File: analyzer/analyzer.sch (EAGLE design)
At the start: 30 parts, among them IC1 FT230XS, J4 ICSP, Q1 16MHz, U1 ATA6631, U2 ATMEGA328P, U4 TLP291, X2 USB-SMD-NS

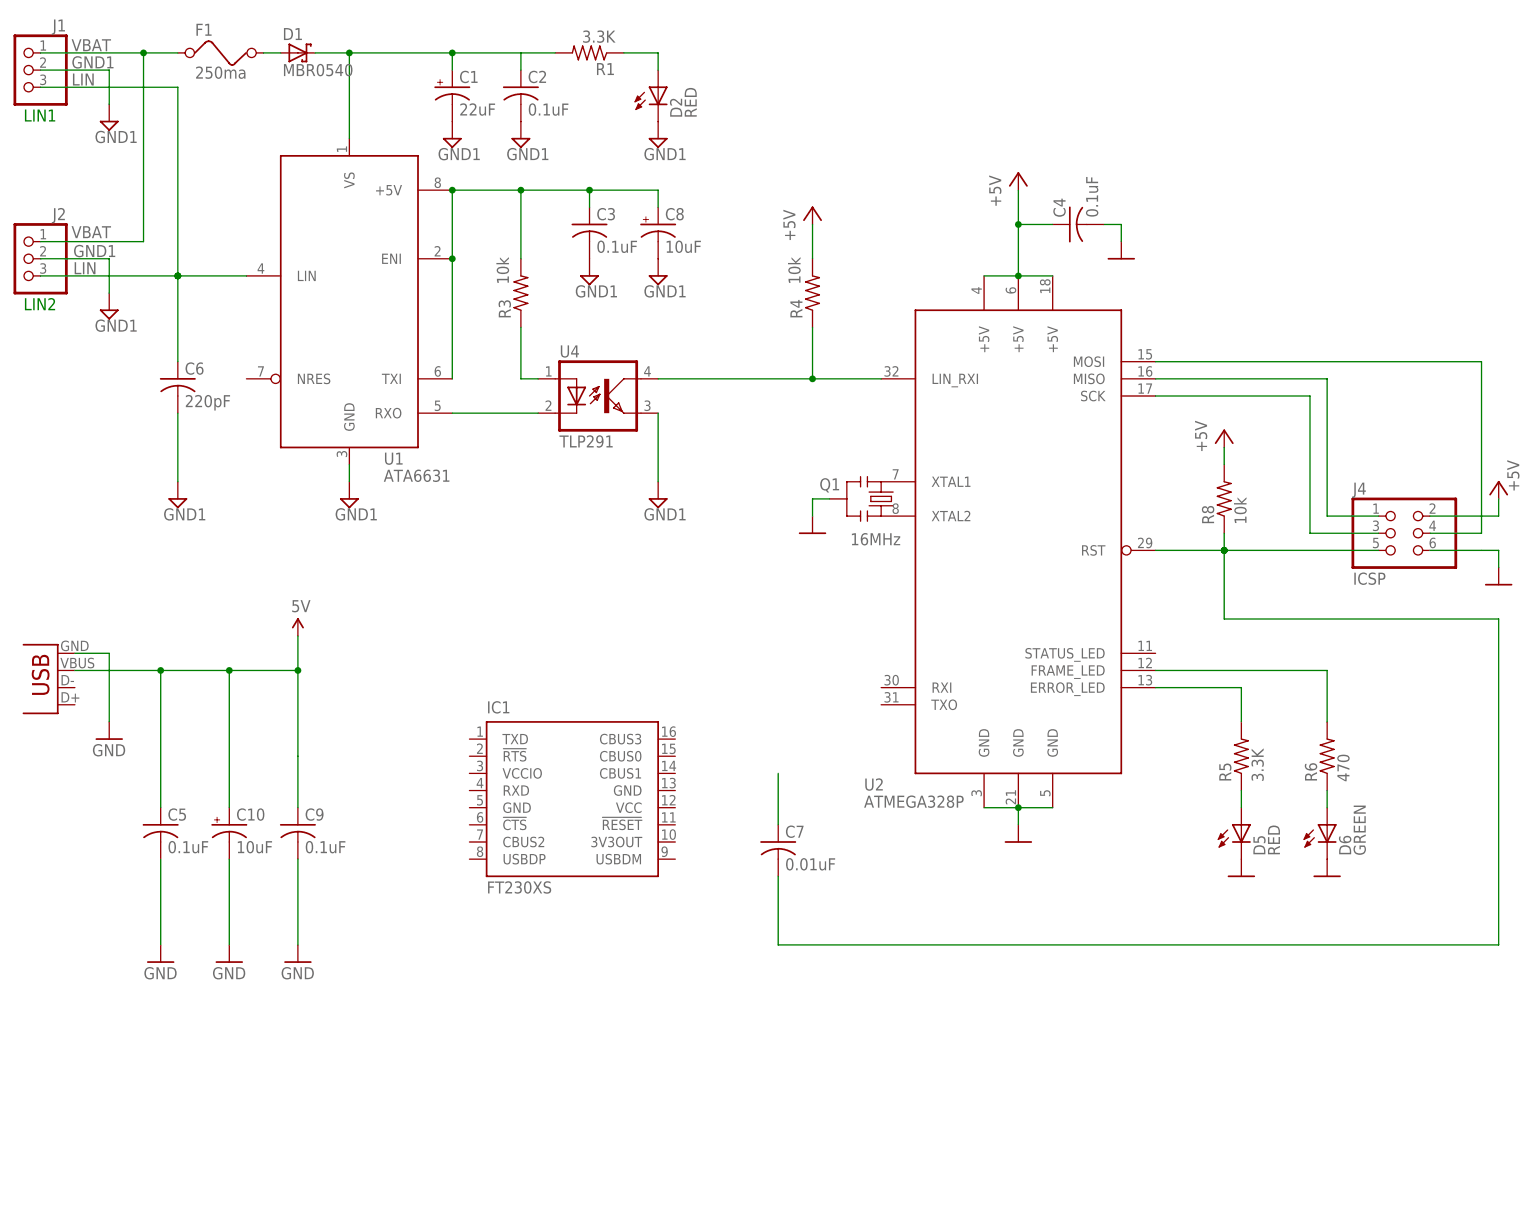
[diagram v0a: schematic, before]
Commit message: Analyzer now can transmit signals to the linbus. Not used yet by the software.
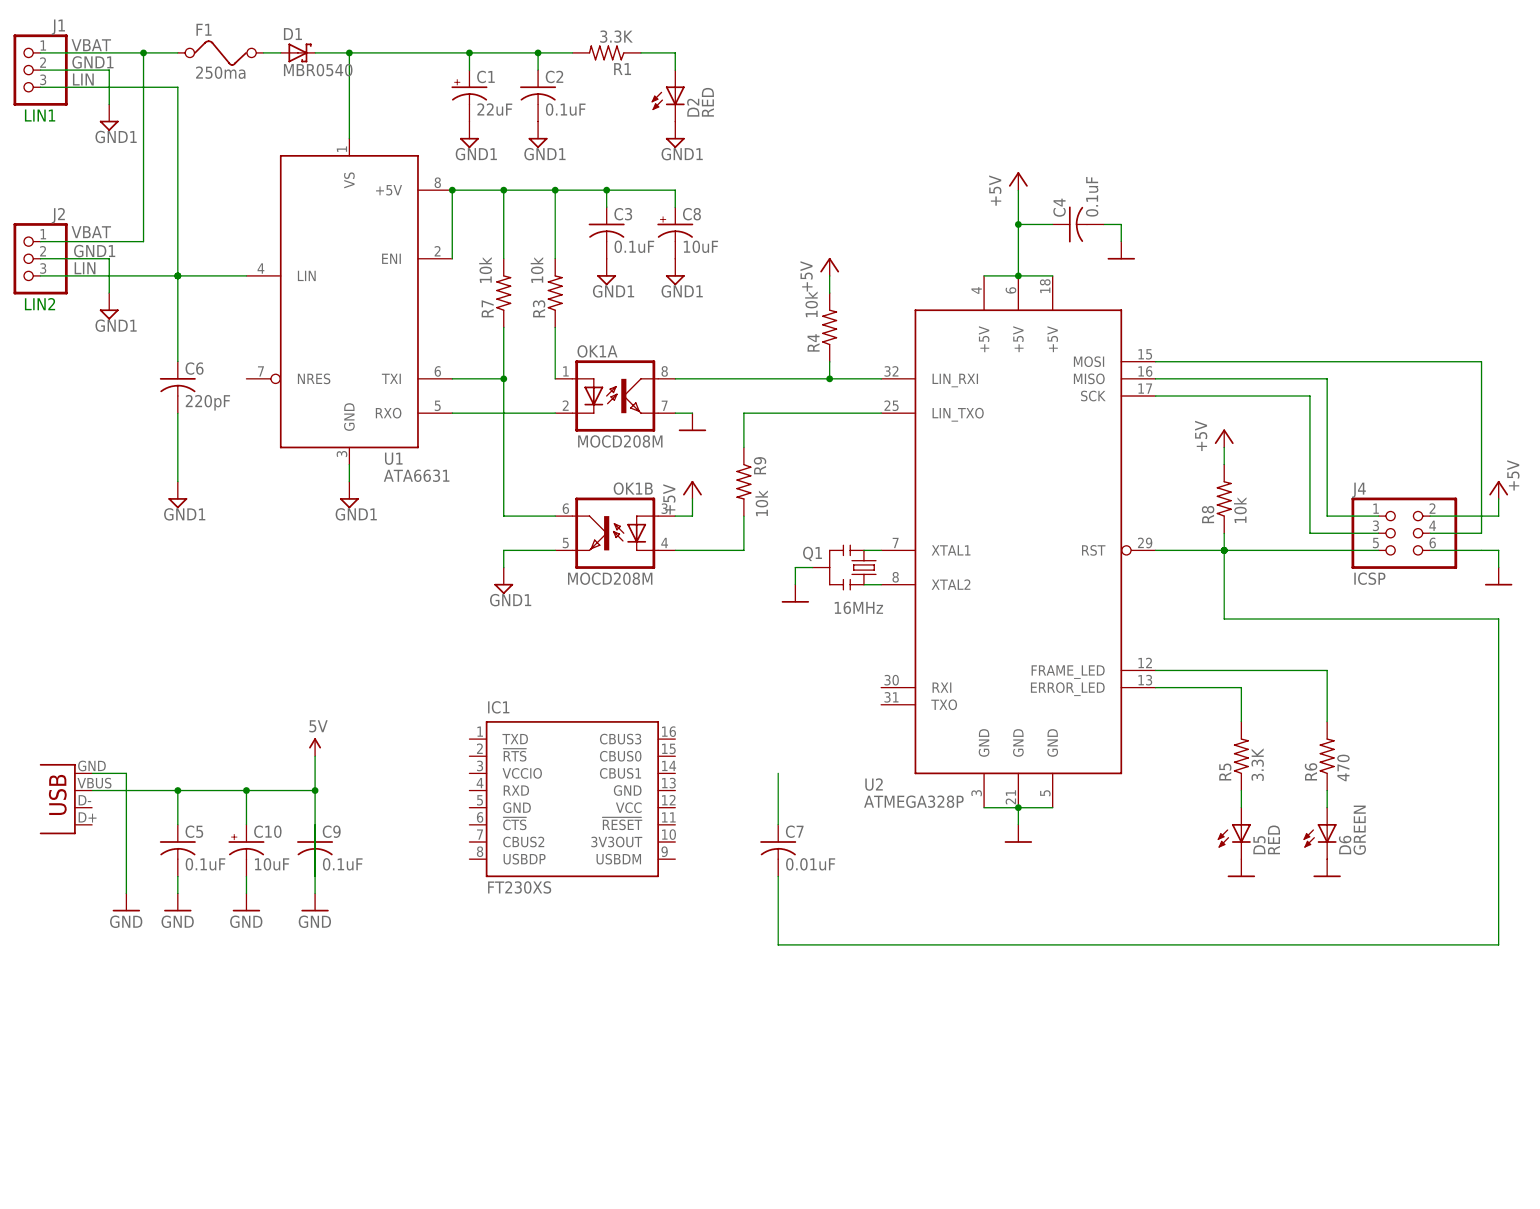
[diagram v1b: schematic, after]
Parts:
- removed U4: TLP291, optocoupler:TLP283
- added OK1: MOCD208M, optocoupler:MOCD208M
- added R7, R9: 10k, rcl:R-US_R0805
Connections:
- new net N$12: OK1B.C, R9.2
- new net N$2: R9.1
- new net N$9: OK1B.COL, R7.1, U1.TXI
- net +5V: now also OK1B.A, R7.2; no longer U1.TXI
- net GND: now also OK1A.EMIT
- net GND1: now also OK1B.EMIT; no longer U4.EMIT
- net N$1: now also OK1A.A; no longer U4.A
- net N$10: now also OK1A.COL; no longer U4.COL
- net N$5: now also OK1A.C; no longer U4.C
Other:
- moved on the sheet: C1, C10, C2, C3, C5, C8, C9, D2, Q1, R1, R3, R4

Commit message: Refactored the analyzer schema.
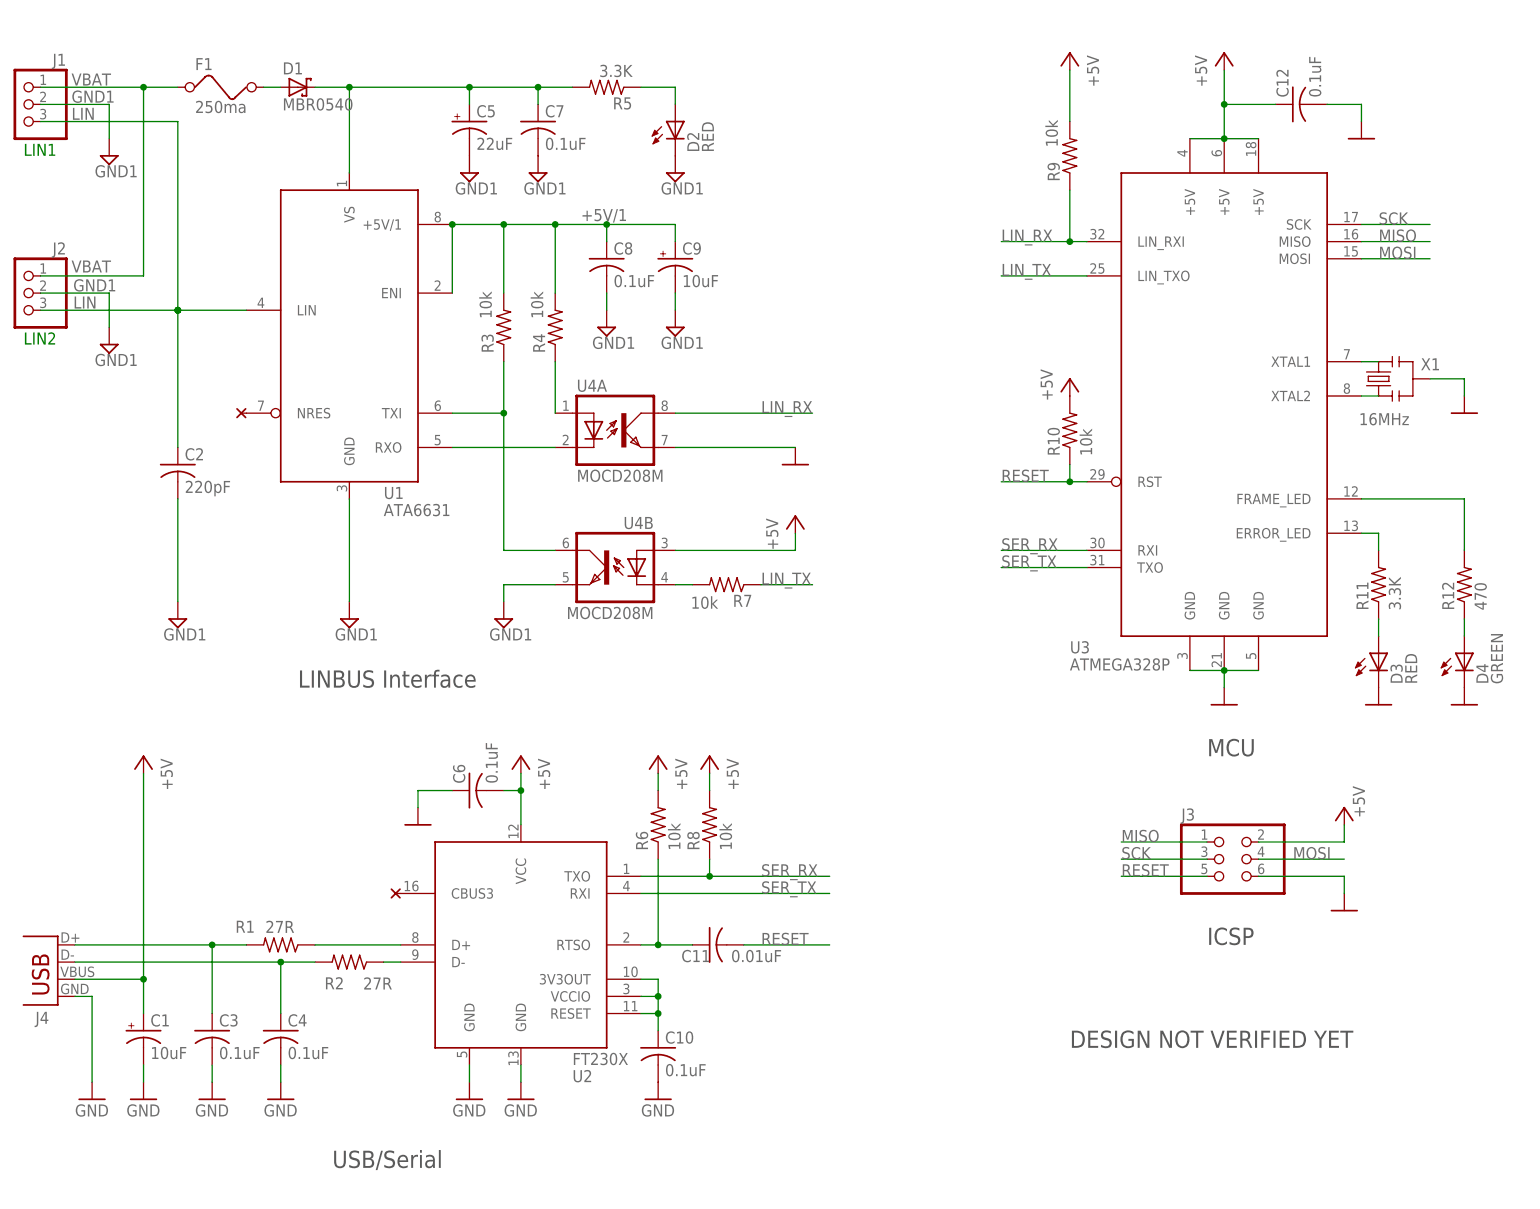
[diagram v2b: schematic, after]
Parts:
- removed D5: RED, led:LEDSMT1206
- removed D6: GREEN, led:LEDSMT1206
- removed IC1: FT230XS, ftdichip:FT230XS
- removed OK1: MOCD208M, optocoupler:MOCD208M
- removed Q1: 16MHz, analyzer:RESONATORSMD
- removed X2: USB-SMD-NS, SparkFun:USB-SMD-NS
- added C11: 0.01uF, rcl:C-USC0805
- added C12: 0.1uF, rcl:C-USC0805
- added D3: RED, led:LEDSMT1206
- added D4: GREEN, led:LEDSMT1206
- added J3: (no value), pinhead:PINHD-2X3
- added R10: 10k, rcl:R-US_R0805
- added R11: 3.3K, rcl:R-US_R0805
- added R12: 470, rcl:R-US_R0805
- added R2: 27R, rcl:R-US_R0805
- added U3: ATMEGA328P, analyzer:ATMEGA328P
- added U4: MOCD208M, optocoupler:MOCD208M
- added X1: 16MHz, analyzer:RESONATORSMD
- C1: value 22uF -> 10uF; device rcl:CPOL-USUD-6,3X5,8 -> rcl:CPOL-USA/3216-18R
- C10, C8: value 10uF -> 0.1uF; device rcl:CPOL-USA/3216-18R -> rcl:C-USC0805
- C2: value 0.1uF -> 220pF
- C5: value 0.1uF -> 22uF; device rcl:C-USC0805 -> rcl:CPOL-USUD-6,3X5,8
- C6: value 220pF -> 0.1uF
- C7: value 0.01uF -> 0.1uF
- C9: value 0.1uF -> 10uF; device rcl:C-USC0805 -> rcl:CPOL-USA/3216-18R
- J4: value ICSP -> USBSMD; device pinhead:PINHD-2X3 -> analyzer:USBSMD
- R1: value 3.3K -> 27R
- R6: value 470 -> 10k
- U2: value ATMEGA328P -> FT230X; device analyzer:ATMEGA328P -> analyzer:FT230X
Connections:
- removed net 3.3V: C9.1
- removed net N$2: R9.1
- removed net N$25: J4.1, U2.MISO
- removed net N$28: J4.3, U2.SCK
- removed net XTAL1: Q1.3, U2.XTAL1
- removed net XTAL2: Q1.1, U2.XTAL2
- new net +5V/1: C8.1, C9.+, R3.2, R4.2, U1.+5V/1, U1.ENI
- new net LIN_RX: R9.1, U3.LIN_RXI, U4A.COL
- new net LIN_TX: R7.1, U3.LIN_TXO
- new net MISO: J3.1, U3.MISO
- new net MOSI: J3.4, U3.MOSI
- new net N$13: U3.XTAL1, X1.3
- new net N$14: U3.XTAL2, X1.1
- new net N$15: C4.1, J4.D-, R2.2
- new net N$18: C10.1, U2.3V3OUT, U2.RESET, U2.VCCIO
- new net RESET: C11.2, J3.5, R10.1, U3.RST
- new net SCK: J3.3, U3.SCK
- new net SER_RX: R8.1, U2.TXO, U3.RXI
- new net SER_TX: U2.RXI, U3.TXO
- net +12V: now also C5.+, C7.1, R5.2; no longer C1.+, C2.1, R1.2
- net +5V: now also C1.+, C12.1, C6.2, J3.2, J4.VBUS, R10.2, R6.2, R9.2, U2.VCC, U3.+5V@1, U3.+5V@2, U3.+5V@3, U4B.A; no longer C10.+, C3.1, C4.1, C5.1, C8.+, J4.2, OK1B.A, R3.2, R4.2, R7.2, U1.+5V, U1.ENI, U2.+5V@1, U2.+5V@2, U2.+5V@3, X2.VBUS
- net GND: now also C1.-, C10.2, C12.2, C3.2, C6.1, D3.C, D4.C, J3.6, J4.GND, U3.GND@1, U3.GND@2, U3.GND@3, U4A.EMIT, X1.2; no longer C10.-, C5.2, C9.2, D5.C, D6.C, J4.6, OK1A.EMIT, Q1.2, U2.GND@3, X2.GND
- net GND1: now also C5.-, C7.2, C8.2, C9.-, U4B.EMIT; no longer C1.-, C3.2, C6.2, C8.-, OK1B.EMIT
- net LIN: now also C2.1; no longer C6.1
- net N$1: now also R4.1, U4A.A; no longer OK1A.A, R3.1
- net N$10: now also C3.1, J4.D+, R1.2; no longer OK1A.COL, R4.1, U2.LIN_RXI
- net N$11: now also R1.1, U2.D+; no longer C7.1
- net N$12: now also R7.2, U4B.C; no longer OK1B.C, R9.2
- net N$16: now also R2.1, U2.D-; no longer C7.2, J4.5, R8.1, U2.RST
- net N$17: now also R5.1; no longer R1.1
- net N$20: now also C11.1, R6.1, U2.RTSO; no longer J4.4, U2.MOSI
- net N$3: now also D4.A, R12.1; no longer D6.A, R6.1
- net N$4: now also D3.A, R11.1; no longer D5.A, R5.1
- net N$5: now also U4A.C; no longer OK1A.C
- net N$7: now also R11.2, U3.ERROR_LED; no longer R5.2, U2.ERROR_LED
- net N$8: now also R12.2, U3.FRAME_LED; no longer R6.2, U2.FRAME_LED
- net N$9: now also R3.1, U4B.COL; no longer OK1B.COL, R7.1
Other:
- note added: "DESIGN NOT VERIFIED YET"
- note added: "ICSP"
- note added: "LINBUS Interface"
- note added: "MCU"
- note added: "USB/Serial"
- moved on the sheet: C1, C2, C3, C4, C6, C7, D1, D2, F1, J1, J2, R1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

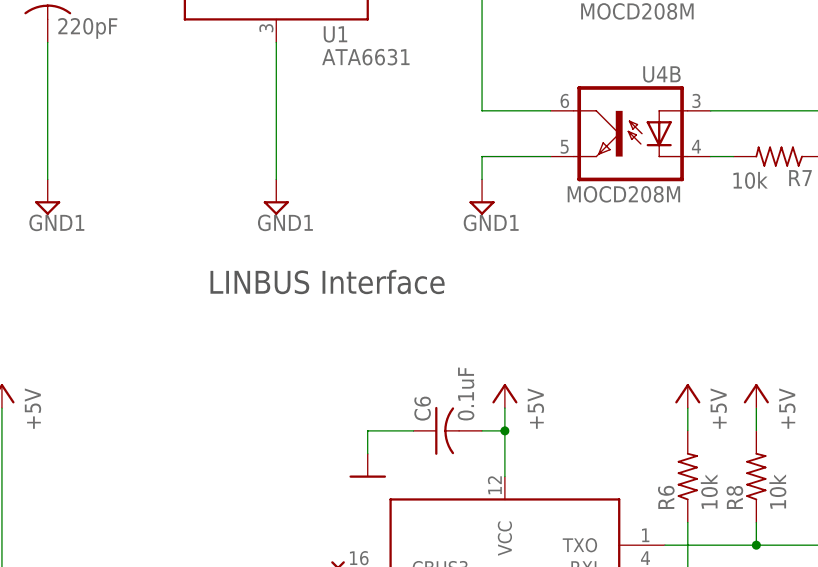
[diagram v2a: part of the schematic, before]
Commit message: Minir text change in analyzer's schema.
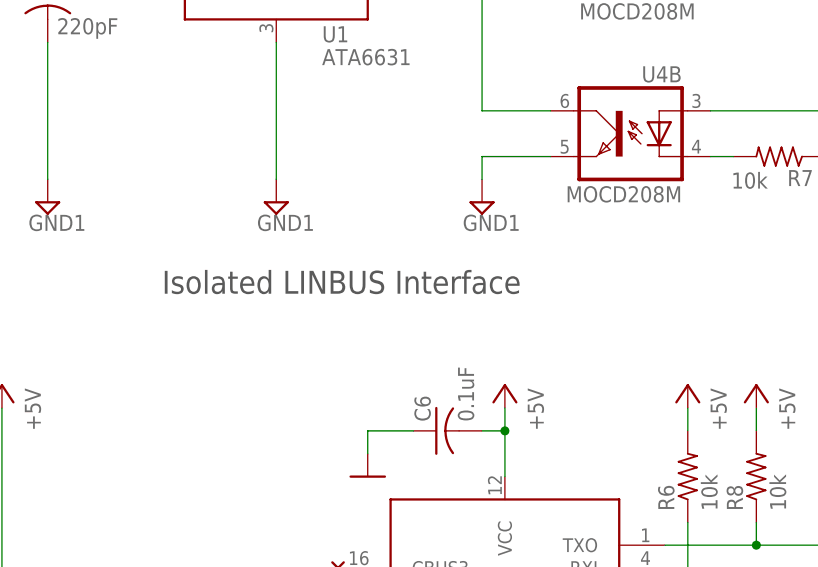
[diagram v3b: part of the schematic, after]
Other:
- note added: "Isolated LINBUS Interface"
- note removed: "LINBUS Interface"
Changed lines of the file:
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@@
 <text x="76.2" y="157.48" size="1.778" layer="91">LIN2</text>
 <text x="121.92" y="35.56" size="2.54" layer="97">USB/Serial</text>
-<text x="116.84" y="106.68" size="2.54" layer="97">LINBUS Interface</text>
+<text x="111.76" y="106.68" size="2.54" layer="97">Isolated LINBUS Interface</text>
 <text x="251.46" y="68.58" size="2.54" layer="97">ICSP</text>
 <text x="251.46" y="96.52" size="2.54" layer="97">MCU</text>

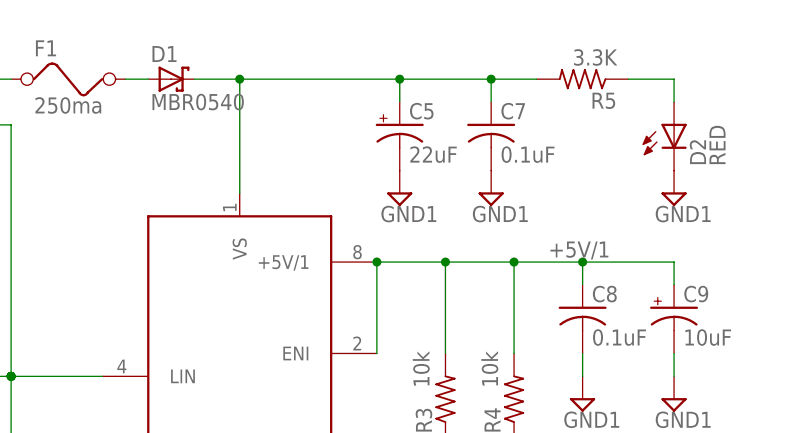
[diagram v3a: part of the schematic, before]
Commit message: Added '40V' annotation to VBAT capacitor.
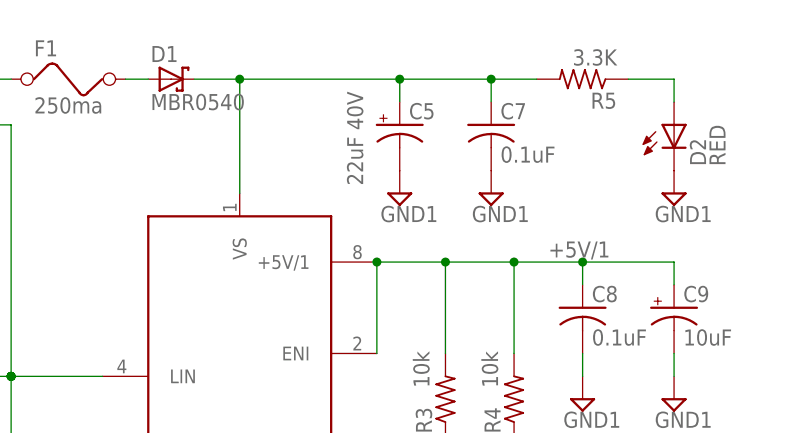
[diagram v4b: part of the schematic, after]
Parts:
- C5: value 22uF -> 22uF 40V
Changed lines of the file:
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@@
 <part name="D3" library="led" deviceset="LED" device="SMT1206" value="RED"/>
 <part name="D4" library="led" deviceset="LED" device="SMT1206" value="GREEN"/>
-<part name="C5" library="rcl" deviceset="CPOL-US" device="UD-6,3X5,8" value="22uF"/>
+<part name="C5" library="rcl" deviceset="CPOL-US" device="UD-6,3X5,8" value="22uF 40V"/>
 <part name="C7" library="rcl" deviceset="C-US" device="C0805" value="0.1uF"/>
 <part name="F1" library="analyzer" deviceset="FUSE" device="" value="250ma"/>
@@
 <instance part="D3" gate="G$1" x="276.86" y="111.76"/>
 <instance part="D4" gate="G$1" x="289.56" y="111.76"/>
-<instance part="C5" gate="G$1" x="142.24" y="190.5"/>
+<instance part="C5" gate="G$1" x="142.24" y="190.5" smashed="yes">
+<attribute name="NAME" x="143.256" y="191.135" size="1.778" layer="95"/>
+<attribute name="VALUE" x="138.176" y="183.769" size="1.778" layer="96" rot="R90"/>
+</instance>
 <instance part="C7" gate="G$1" x="152.4" y="190.5"/>
 <instance part="F1" gate="G$1" x="106.68" y="195.58"/>
@@
 <instance part="SUPPLY1" gate="G$1" x="88.9" y="157.48"/>
 <instance part="SUPPLY2" gate="G$1" x="88.9" y="185.42"/>
-<instance part="SUPPLY3" gate="G$1" x="142.24" y="182.88"/>
+<instance part="SUPPLY3" gate="G$1" x="142.24" y="182.88" smashed="yes">
+<attribute name="VALUE" x="140.081" y="179.705" size="1.778" layer="96"/>
+</instance>
 <instance part="SUPPLY4" gate="G$1" x="152.4" y="182.88"/>
 <instance part="SUPPLY5" gate="G$1" x="99.06" y="116.84"/>
